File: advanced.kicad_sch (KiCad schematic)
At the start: 28 parts, among them U1 ATtiny24-20P, U2 ATtiny28L-4P, U3 ATtiny13A-P, U4 ATtiny25-20P, U5 ATtiny24-20P, U6 ATtiny85-20P

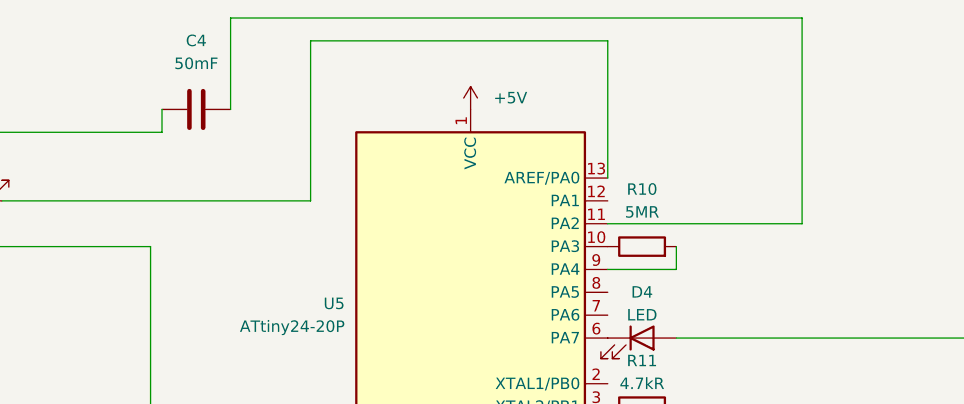
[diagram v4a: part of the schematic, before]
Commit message: board shrunk to 10*10 , all pads now round
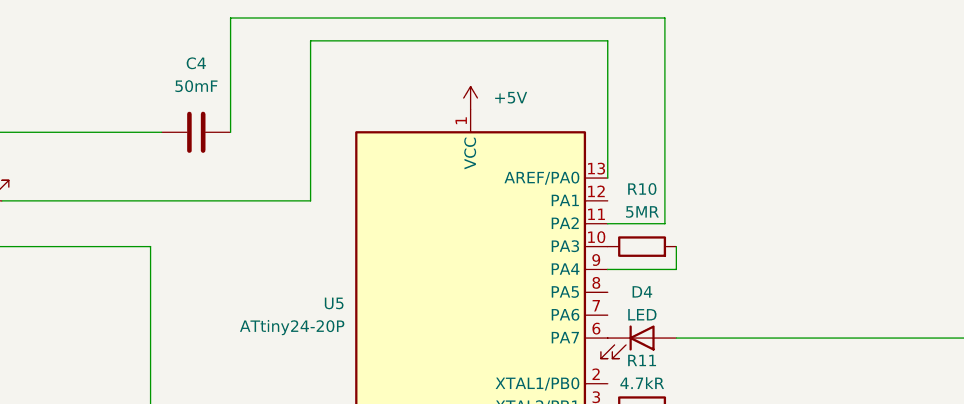
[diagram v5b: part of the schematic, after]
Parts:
- C5, C6, C8: footprint Capacitor_THT:CP_Axial_L10.0mm_D4.5mm_P15.00mm_Horizontal -> Capacitor_THT:CP_Radial_D6.3mm_P2.50mm
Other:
- moved on the sheet: C4
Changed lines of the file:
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@@
   (junction (at 83.82 123.19) (diameter 0) (color 0 0 0 0)
   )
-  (wire (pts (xy 172.72 41.91) (xy 172.72 39.37))
-    (stroke (width 0) (type default) (color 0 0 0 0))
-  )
   (wire (pts (xy 196.85 124.46) (xy 185.42 124.46))
     (stroke (width 0) (type default) (color 0 0 0 0))
@@
     (stroke (width 0) (type default) (color 0 0 0 0))
   )
-  (wire (pts (xy 243.84 52.07) (xy 222.25 52.07))
+  (wire (pts (xy 228.6 52.07) (xy 222.25 52.07))
     (stroke (width 0) (type default) (color 0 0 0 0))
   )
@@
     (stroke (width 0) (type default) (color 0 0 0 0))
   )
-  (wire (pts (xy 180.34 29.21) (xy 243.84 29.21))
+  (wire (pts (xy 180.34 29.21) (xy 228.6 29.21))
     (stroke (width 0) (type default) (color 0 0 0 0))
   )
@@
     (stroke (width 0) (type default) (color 0 0 0 0))
   )
-  (wire (pts (xy 180.34 39.37) (xy 180.34 29.21))
+  (wire (pts (xy 180.34 41.91) (xy 180.34 29.21))
     (stroke (width 0) (type default) (color 0 0 0 0))
   )
@@
     (stroke (width 0) (type default) (color 0 0 0 0))
   )
-  (wire (pts (xy 243.84 29.21) (xy 243.84 52.07))
+  (wire (pts (xy 228.6 29.21) (xy 228.6 52.07))
     (stroke (width 0) (type default) (color 0 0 0 0))
   )
@@
       (effects (font (size 1.27 1.27)) (justify left))
     )
-    (property "Footprint" "Capacitor_THT:CP_Axial_L10.0mm_D4.5mm_P15.00mm_Horizontal" (id 2) (at 204.1652 106.68 0)
+    (property "Footprint" "Capacitor_THT:CP_Radial_D6.3mm_P2.50mm" (id 2) (at 204.1652 106.68 0)
       (effects (font (size 1.27 1.27)) hide)
     )
@@
       (effects (font (size 1.27 1.27)) (justify left))
     )
-    (property "Footprint" "Capacitor_THT:CP_Axial_L10.0mm_D4.5mm_P15.00mm_Horizontal" (id 2) (at 222.25 78.4352 0)
+    (property "Footprint" "Capacitor_THT:CP_Radial_D6.3mm_P2.50mm" (id 2) (at 222.25 78.4352 0)
       (effects (font (size 1.27 1.27)) hide)
     )
@@
       (effects (font (size 1.27 1.27)) (justify left))
     )
-    (property "Footprint" "Capacitor_THT:CP_Axial_L10.0mm_D4.5mm_P15.00mm_Horizontal" (id 2) (at 193.04 128.5748 0)
+    (property "Footprint" "Capacitor_THT:CP_Radial_D6.3mm_P2.50mm" (id 2) (at 193.04 128.5748 0)
       (effects (font (size 1.27 1.27)) hide)
     )
@@
     (pin "2")
   )
-  (symbol (lib_id "Device:C") (at 176.53 39.37 270) (unit 1)
-    (in_bom yes) (on_board yes) (fields_autoplaced)
-    (property "Reference" "C4" (id 0) (at 176.53 31.75 90))
-    (property "Value" "50mF" (id 1) (at 176.53 34.29 90))
-    (property "Footprint" "Capacitor_THT:C_Disc_D3.4mm_W2.1mm_P2.50mm" (id 2) (at 172.72 40.3352 0)
-      (effects (font (size 1.27 1.27)) hide)
-    )
-    (property "Datasheet" "~" (id 3) (at 176.53 39.37 0)
+  (symbol (lib_id "Device:C") (at 176.53 41.91 270) (unit 1)
+    (in_bom yes) (on_board yes) (fields_autoplaced)
+    (property "Reference" "C4" (id 0) (at 176.53 34.29 90))
+    (property "Value" "50mF" (id 1) (at 176.53 36.83 90))
+    (property "Footprint" "Capacitor_THT:C_Disc_D3.4mm_W2.1mm_P2.50mm" (id 2) (at 172.72 42.8752 0)
+      (effects (font (size 1.27 1.27)) hide)
+    )
+    (property "Datasheet" "~" (id 3) (at 176.53 41.91 0)
       (effects (font (size 1.27 1.27)) hide)
     )
@@
     )
     (path "/f6378489-314e-44ab-8ad8-987bd0c8d278"
-      (reference "C5") (unit 1) (value "100mF") (footprint "Capacitor_THT:CP_Axial_L10.0mm_D4.5mm_P15.00mm_Horizontal")
+      (reference "C5") (unit 1) (value "100mF") (footprint "Capacitor_THT:CP_Radial_D6.3mm_P2.50mm")
     )
     (path "/11860a85-ef01-4ce2-a8d5-5d0001d777de"
-      (reference "C6") (unit 1) (value "100mF") (footprint "Capacitor_THT:CP_Axial_L10.0mm_D4.5mm_P15.00mm_Horizontal")
+      (reference "C6") (unit 1) (value "100mF") (footprint "Capacitor_THT:CP_Radial_D6.3mm_P2.50mm")
     )
     (path "/c771b298-f03d-481f-9bb4-2d748e4fee4e"
-      (reference "C8") (unit 1) (value "100mF") (footprint "Capacitor_THT:CP_Axial_L10.0mm_D4.5mm_P15.00mm_Horizontal")
+      (reference "C8") (unit 1) (value "100mF") (footprint "Capacitor_THT:CP_Radial_D6.3mm_P2.50mm")
     )
     (path "/b521407b-f4cd-489f-ab91-97ddaa13d7e8"
